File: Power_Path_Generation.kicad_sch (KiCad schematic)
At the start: 11 parts, among them Q701 PMOS SI2365EDS-T1-GE3, U701 TPS3839G33DQNR, U702 TPS7A0233DBVR

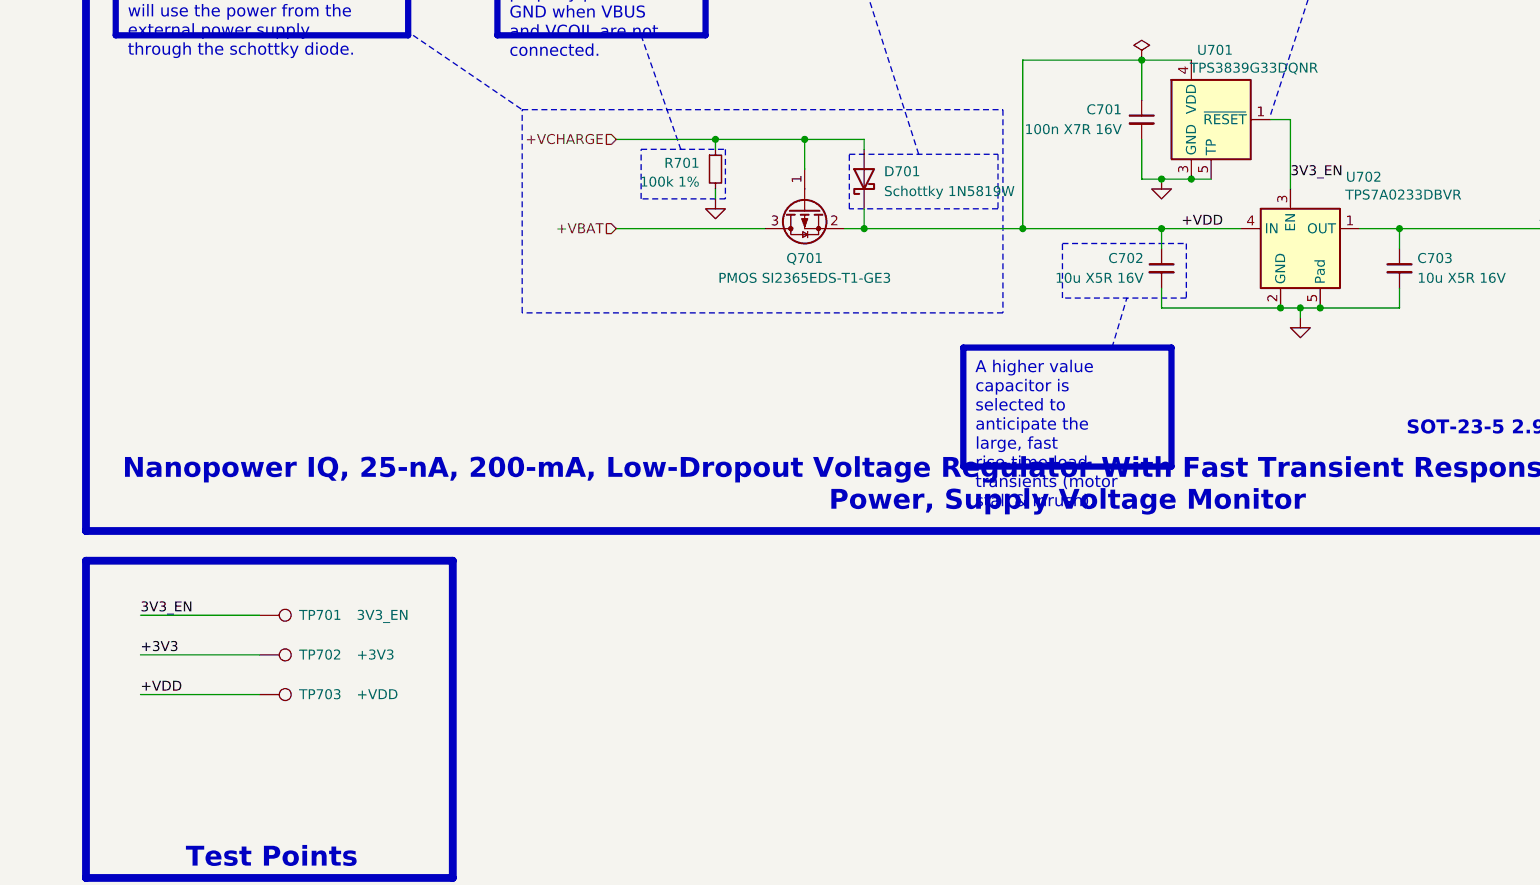
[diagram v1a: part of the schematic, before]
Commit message: Added PCB frame for assembly, almost finished auto-review, only MCU and motors left
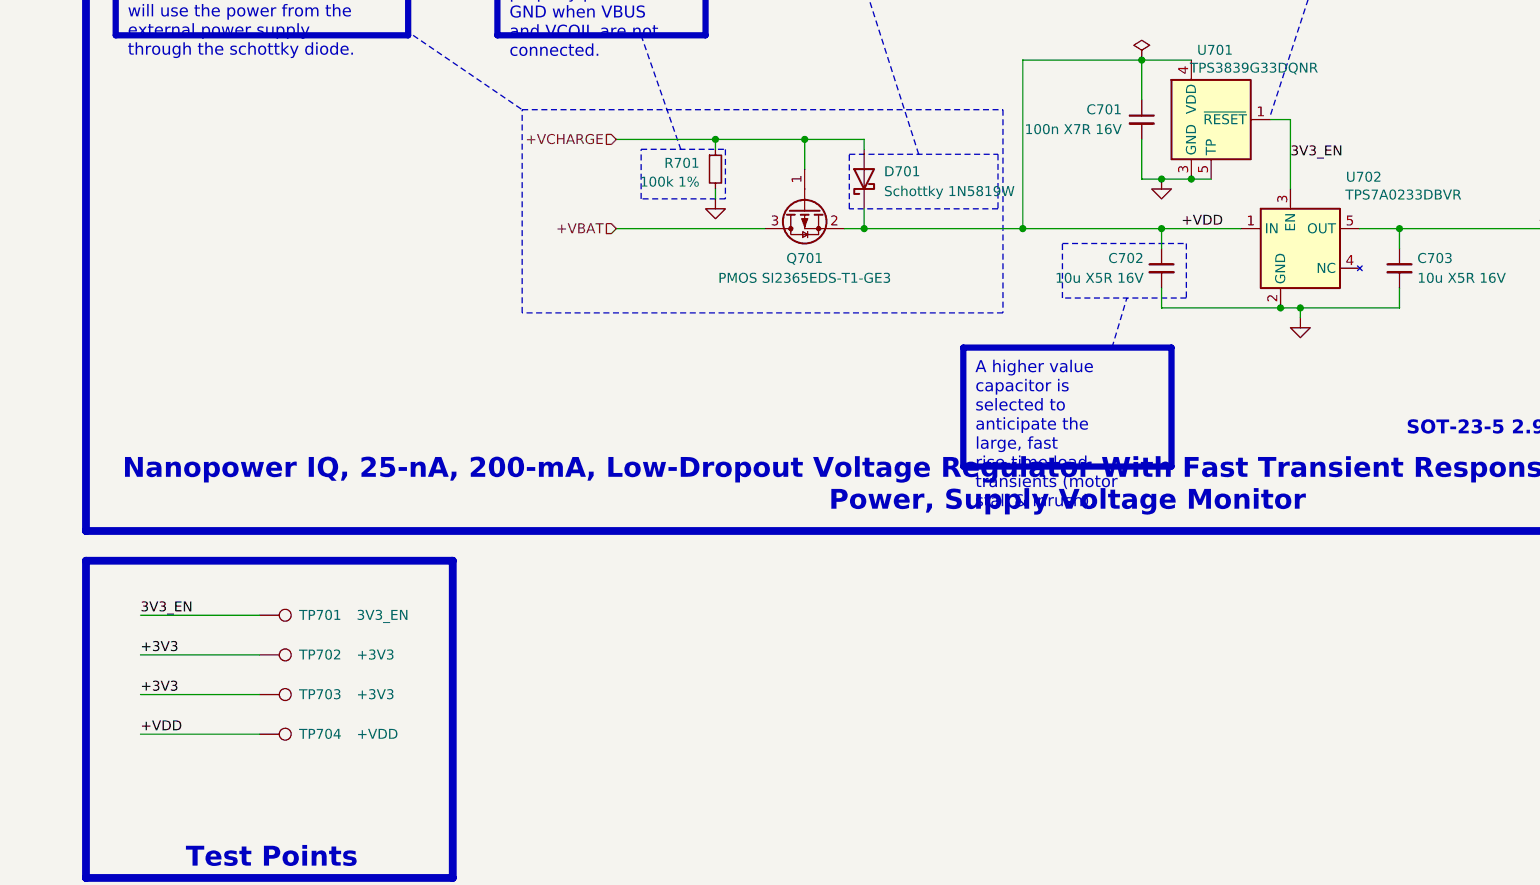
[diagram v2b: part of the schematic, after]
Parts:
- added TP703: +3V3, TestPoint:TestPoint_THTPad_D1.5mm_Drill0.7mm, symbol Connector:TestPoint
- D701: footprint Diode_SMD:Nexperia_CFP3_SOD-123W -> 0_Plume:Nexperia_CFP3_SOD-123W
- TP701: footprint 0_Plume:TestPoint_Pad_D0.5mm_Back -> 0_Plume:TestPoint_Pad_D0.5mm_Front
- TP702: footprint 0_Plume:TestPoint_Pad_D0.5mm_Back -> 0_Plume:TestPoint_Pad_D0.75mm_Front
- TP704: renamed from TP703; footprint 0_Plume:TestPoint_Pad_D0.5mm_Back -> 0_Plume:TestPoint_Pad_D0.5mm_Front
- U702: footprint Package_TO_SOT_SMD:SOT-23-5 -> 0_Plume:SOT-23-5-TEXAS; symbol 0_Plume:TPS7A20xxxDBVR -> 0_Plume:TPS7A02xxxDBVR
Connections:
- net +3V3: now also U702.5 (OUT), TP703.1; no longer U702.1 (OUT)
- net +VDD: now also U702.1 (IN); no longer U702.4 (IN)
- net GND: no longer U702.5 (Pad)
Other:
- moved on the sheet: TP704
